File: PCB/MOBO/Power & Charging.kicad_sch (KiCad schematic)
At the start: 53 parts, among them J201 MAIN-USBC-OTG/PWR, Q201 AO3401A, Q202 FS8205A, Q203 IRLML6344, Q204 Si4435DDY, SW201 PCM12SMTR, U201 DW01A, U202 LC709203FQH-01TWG, U203 MCP73871-1AA, U204 TPS61230DRC

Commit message: added parts links in BOM
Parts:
- F201: footprint Fuse:Fuse_0805_2012Metric -> Fuse:Fuse_1206_3216Metric
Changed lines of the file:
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@@
       (effects (font (size 1.27 1.27)) hide)
     )
-    (property "Datasheet" "~" (at 179.07 209.55 0)
+    (property "Datasheet" "https://octopart.com/ncu18xh103f6srb-murata-75166631?r=sp" (at 179.07 209.55 0)
       (effects (font (size 1.27 1.27)) hide)
     )
@@
       (effects (font (size 1.27 1.27)) hide)
     )
-    (property "Datasheet" "~" (at 260.35 92.71 0)
+    (property "Datasheet" "https://octopart.com/pcm12smtr-c%26k+components-2486974?r=sp" (at 260.35 92.71 0)
       (effects (font (size 1.27 1.27)) hide)
     )
@@
       (effects (font (size 1.27 1.27)) hide)
     )
-    (property "Datasheet" "~" (at 196.85 69.85 0)
+    (property "Datasheet" "https://octopart.com/vaol-s8wr4-vcc-11855073?r=sp" (at 196.85 69.85 0)
       (effects (font (size 1.27 1.27)) hide)
     )
@@
       (effects (font (size 1.27 1.27)))
     )
-    (property "Footprint" "Fuse:Fuse_0805_2012Metric" (at 58.42 38.608 90)
-      (effects (font (size 1.27 1.27)) hide)
-    )
-    (property "Datasheet" "~" (at 58.42 36.83 0)
+    (property "Footprint" "Fuse:Fuse_1206_3216Metric" (at 58.42 38.608 90)
+      (effects (font (size 1.27 1.27)) hide)
+    )
+    (property "Datasheet" "https://octopart.com/0437002.wr-littelfuse-8600120?r=sp" (at 58.42 36.83 0)
       (effects (font (size 1.27 1.27)) hide)
     )
@@
       (effects (font (size 1.27 1.27)) hide)
     )
-    (property "Datasheet" "~" (at 179.07 68.58 0)
+    (property "Datasheet" "https://octopart.com/598-8191-107f-dialight-868609?r=sp" (at 179.07 68.58 0)
       (effects (font (size 1.27 1.27)) hide)
     )
@@
       (effects (font (size 1.27 1.27)) hide)
     )
-    (property "Datasheet" "https://www.usb.org/sites/default/files/documents/usb_type-c.zip" (at 31.75 52.07 0)
+    (property "Datasheet" "https://octopart.com/usb4085-gf-a-global+connector+technology-94773699?r=sp" (at 31.75 52.07 0)
       (effects (font (size 1.27 1.27)) hide)
     )
@@
       (effects (font (size 1.27 1.27)) hide)
     )
-    (property "Datasheet" "~" (at 134.62 91.44 0)
+    (property "Datasheet" "https://octopart.com/ncu18xh103f6srb-murata-75166631?r=sp" (at 134.62 91.44 0)
       (effects (font (size 1.27 1.27)) hide)
     )
@@
       (effects (font (size 1.27 1.27)) hide)
     )
-    (property "Datasheet" "~" (at 186.69 69.85 0)
-      (effects (font (size 1.27 1.27)) hide)
-    )
+    (property "Datasheet" "https://octopart.com/598-8120-107f-dialight-868603?r=sp" (at 186.69 69.85 0)
+      (effects (font (size 1.27 1.27)) hide)
+    )

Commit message: fixed schematic net names
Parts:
- J201: footprint Connector_USB:USB_C_Receptacle_GCT_USB4085 -> Connector_USB:USB_C_Receptacle_G-Switch_GT-USB-7010ASV
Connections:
- net +3V8: no longer C205.1, C206.1, Q204.5 (D), Q204.6 (D), Q204.7 (D), Q204.8 (D), R218.1, U203.1 (OUT), U203.20 (OUT)
- net +5V: no longer C202.1, F201.1, J201.A4 (VBUS), J201.A9 (VBUS), J201.B4 (VBUS), J201.B9 (VBUS), Q201.2 (S), R205.1, R207.1, U203.17 (CE), U203.18 (IN), U203.19 (IN), U203.4 (PROG2)
- net VPCC: now reaches R207.2, R208.1, U203.2 (VPCC)
- net PG: now reaches D203.2 (A), U203.6 (~{PG})
- net STAT2: now reaches D201.2 (A), U203.7 (STAT2)
- net STAT1: now reaches D202.2 (A), U203.8 (STAT1/~{LBO})
- net Latch Hold: now reaches D204.2 (A), Q203.1 (G), R217.2, R219.1
- net +5VA: now reaches D206.5 (VP), F201.2, Q201.3 (D)
- net Latch Enable: now reaches C206.2, D205.2 (A), Q203.3 (D), Q204.4 (G), R218.2
- net D+_IN: now reaches D206.1 (L1), J201.A7 (D-), J201.B7 (D-)
- net D-_IN: now reaches D206.3 (L2), J201.A6 (D+), J201.B6 (D+)
- new net +5VD: C202.1, Q201.2 (S), R205.1, R207.1, U203.17 (CE), U203.18 (IN), U203.19 (IN), U203.4 (PROG2)
- new net Charger 3V8 out: C205.1, C206.1, Q204.5 (D), Q204.6 (D), Q204.7 (D), Q204.8 (D), R218.1, U203.1 (OUT), U203.20 (OUT)
- new net VBUS: F201.1, J201.A4 (VBUS), J201.A9 (VBUS), J201.B4 (VBUS), J201.B9 (VBUS)
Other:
- moved on the sheet: R205

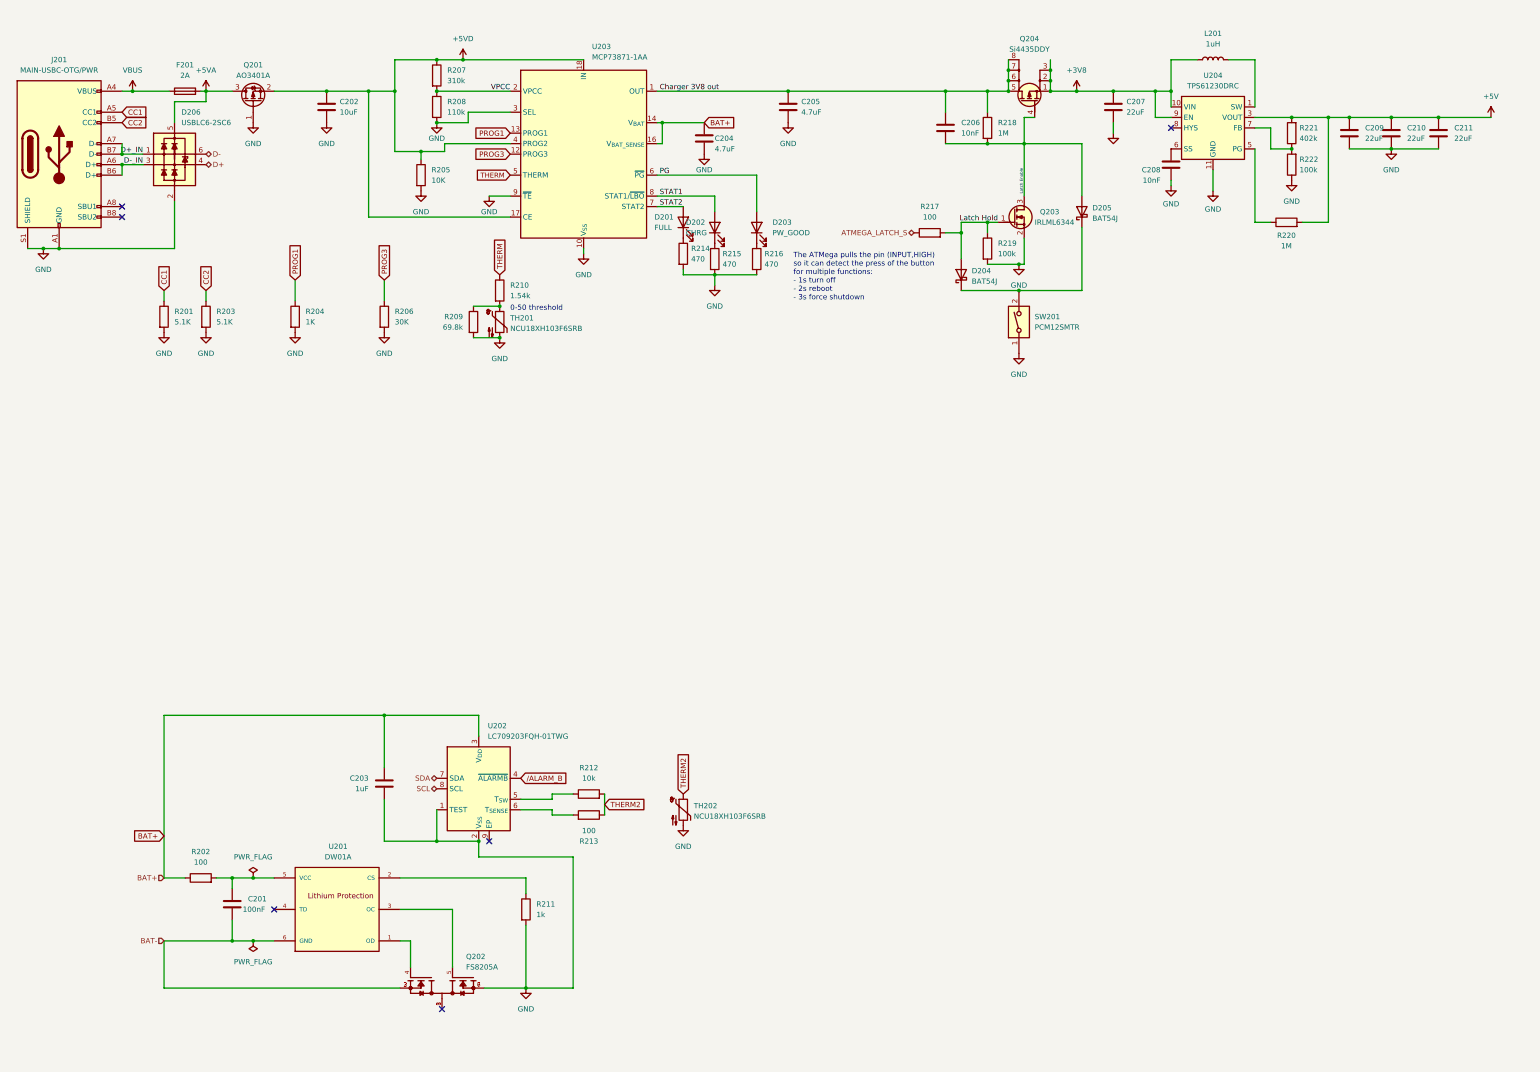
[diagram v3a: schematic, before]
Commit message: Started pcb traces
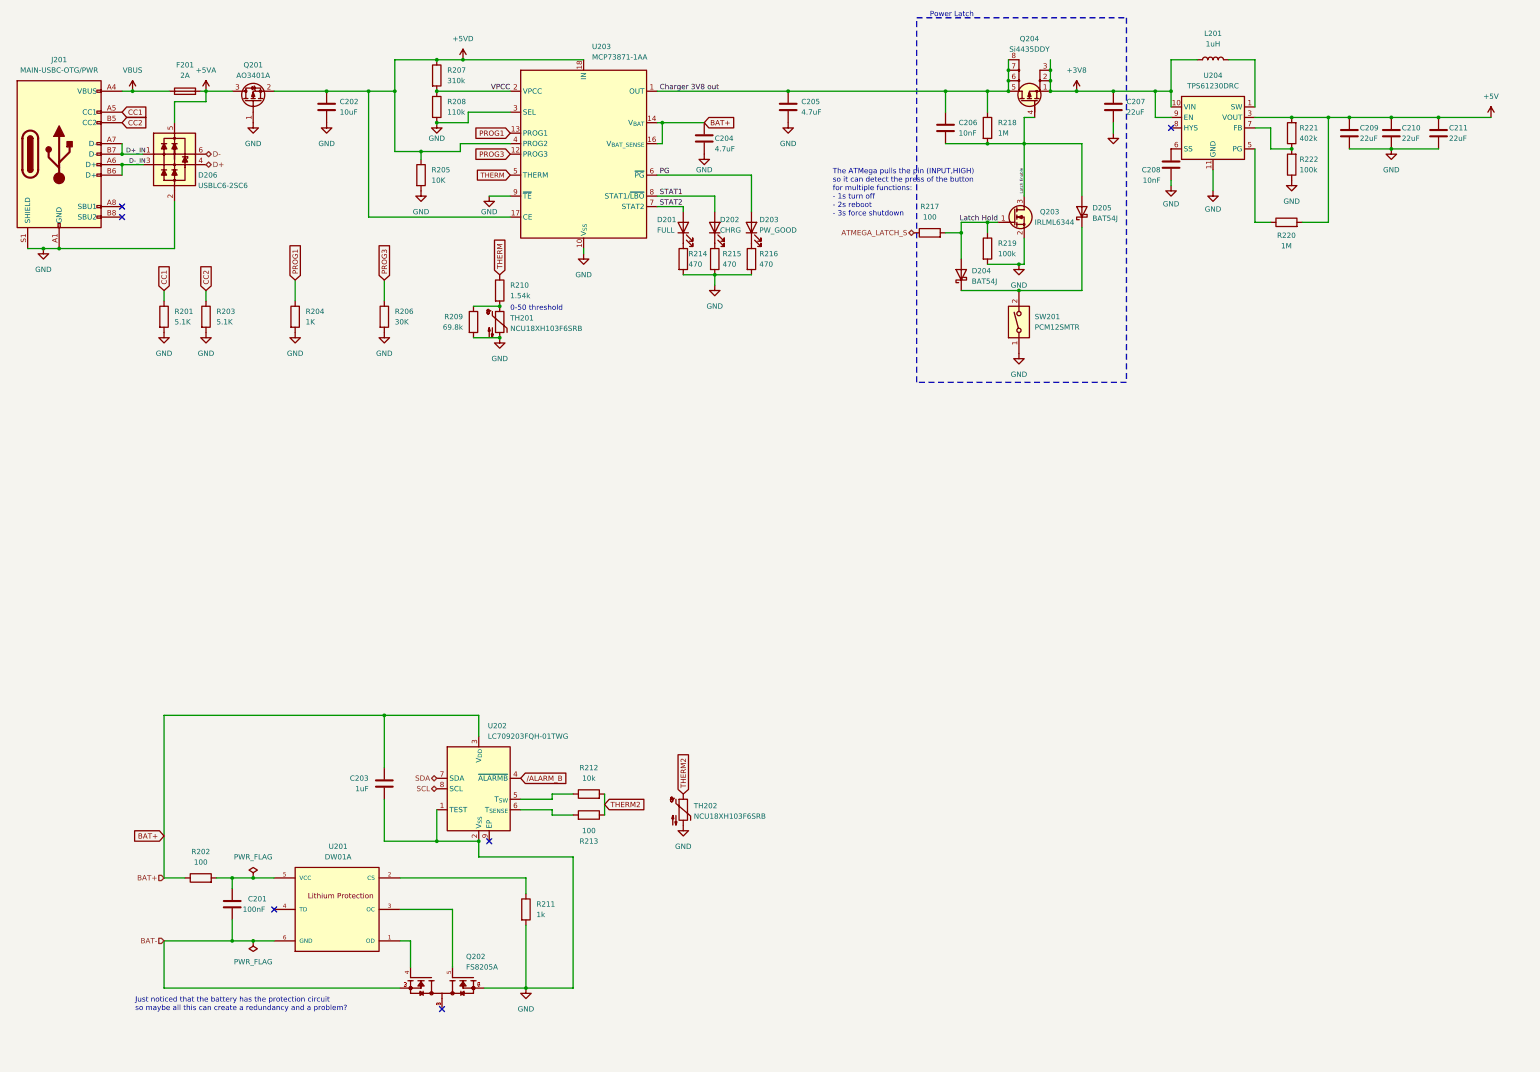
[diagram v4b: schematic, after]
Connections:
- net D+_IN: no longer D206.1 (L1), J201.A7 (D-), J201.B7 (D-)
- net D-_IN: no longer D206.3 (L2), J201.A6 (D+), J201.B6 (D+)
- new net: D206.1 (L1), J201.A7 (D-), J201.B7 (D-)
- new net: D206.3 (L2), J201.A6 (D+), J201.B6 (D+)
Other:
- note added: "Just noticed that the battery has the protection circuit so maybe all this can create a redundancy and a problem?"
- note added: "Power Latch"
- title: (none) -> Power & Charging
- moved on the sheet: D201, D203, R214, R216

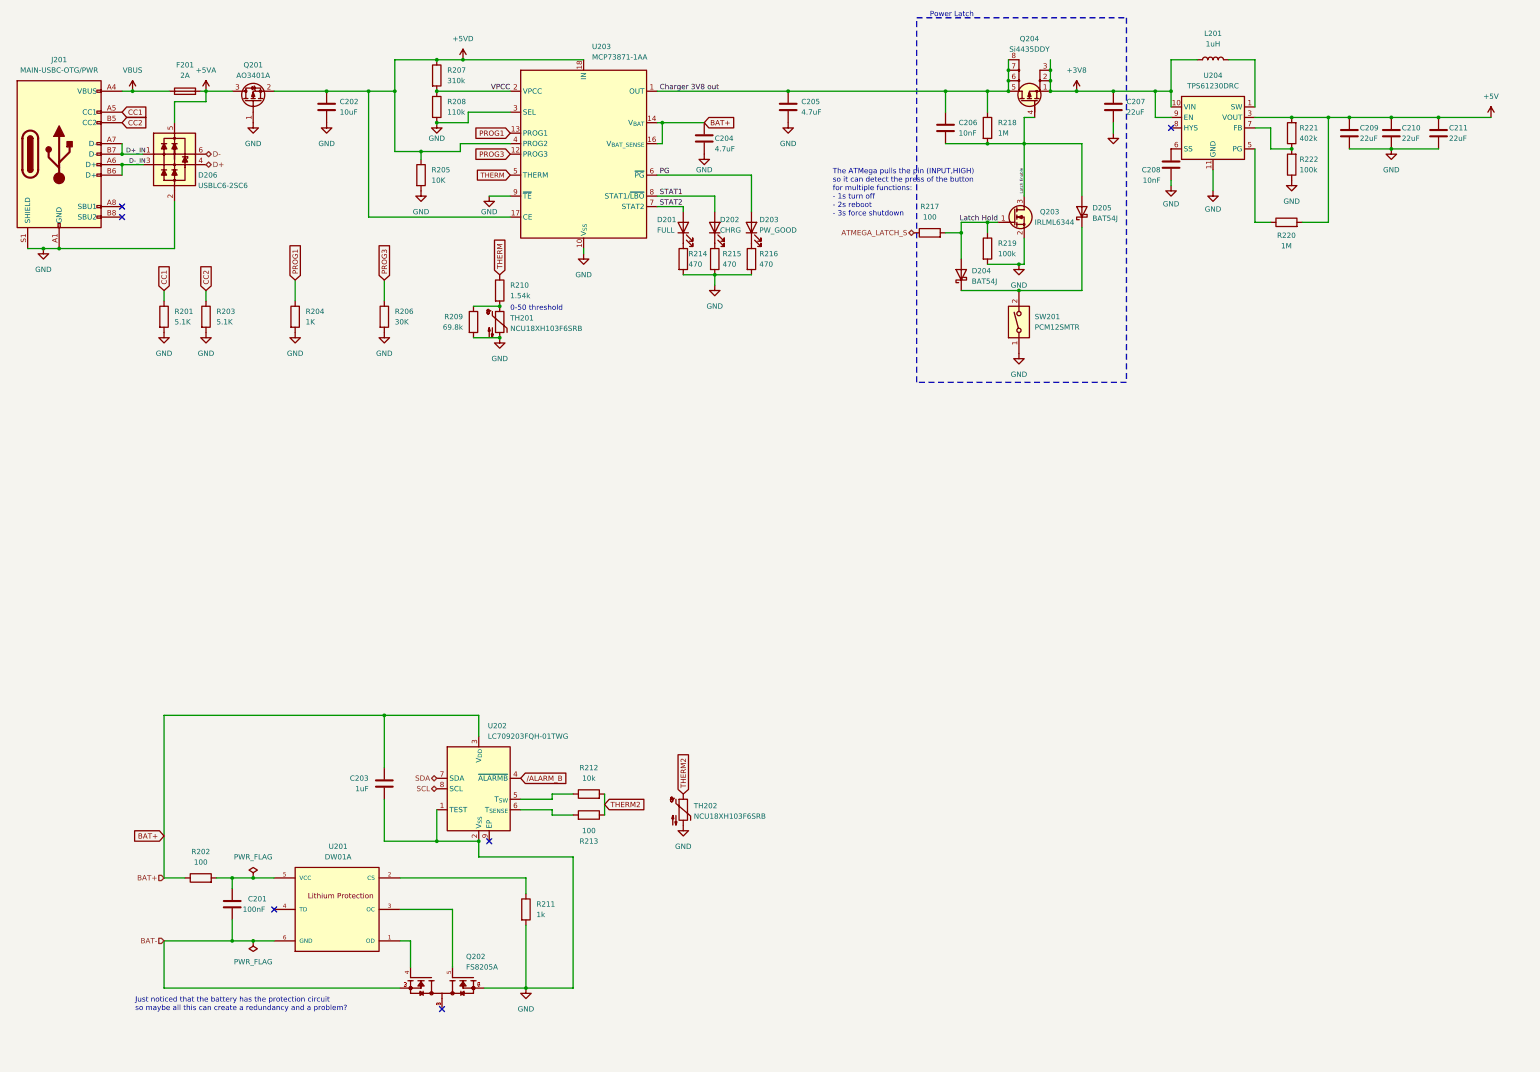
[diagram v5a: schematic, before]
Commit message: removed battery protection and gauge circuit
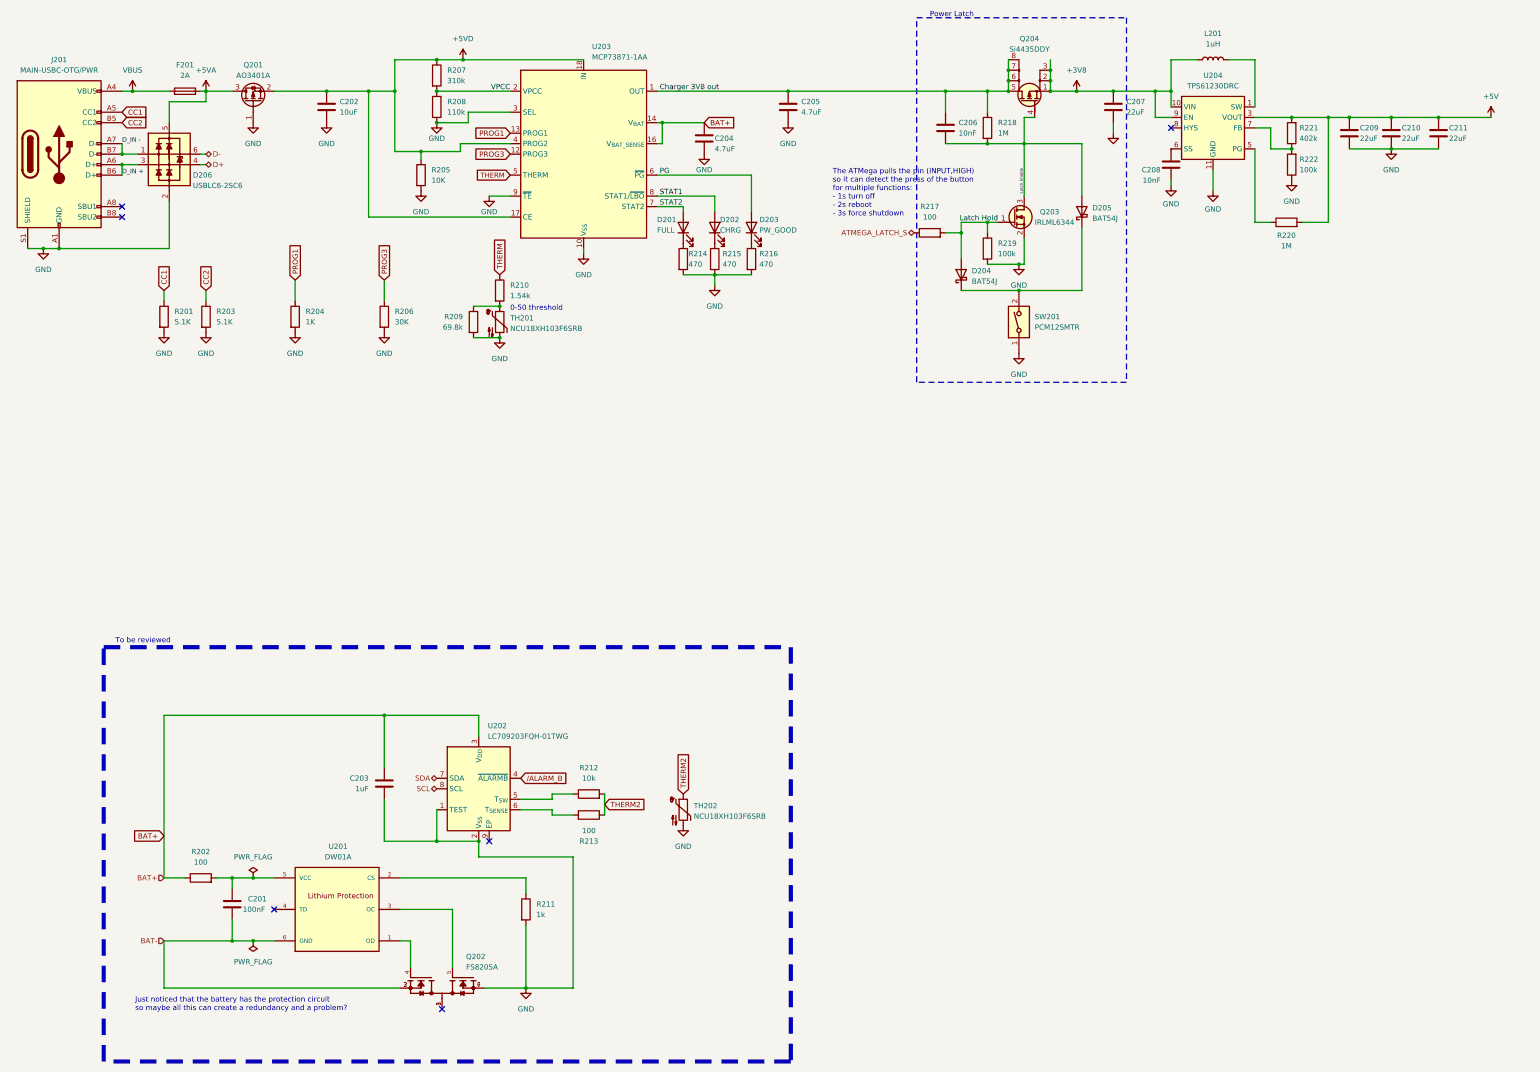
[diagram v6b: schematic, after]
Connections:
- net D_IN -: now reaches D206.1 (L1), J201.A7 (D-), J201.B7 (D-)
- net D_IN +: now reaches D206.3 (L2), J201.A6 (D+), J201.B6 (D+)
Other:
- note added: "To be reviewed"
- moved on the sheet: D206
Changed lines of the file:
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@@
 	)
 	(junction
+		(at 43.18 54.61)
+		(diameter 0)
+		(color 0 0 0 0)
+	)
+	(junction
 		(at 109.22 36.83)
 		(diameter 0)
@@
 	)
 	(junction
-		(at 43.18 54.61)
-		(diameter 0)
-		(color 0 0 0 0)
-	)
-	(junction
 		(at 350.52 43.18)
 		(diameter 0)
@@
 	(wire
 		(pts
+			(xy 62.23 52.07) (xy 63.5 52.07)
+		)
+		(stroke
+			(width 0)
+			(type default)
+		)
+	)
+	(wire
+		(pts
 			(xy 58.42 227.33) (xy 53.34 227.33)
 		)
@@
 	(wire
 		(pts
-			(xy 43.18 54.61) (xy 48.26 54.61)
-		)
-		(stroke
-			(width 0)
-			(type default)
-		)
-	)
-	(wire
-		(pts
 			(xy 139.7 208.28) (xy 147.32 208.28)
 		)
@@
 	(wire
 		(pts
-			(xy 43.18 52.07) (xy 48.26 52.07)
-		)
-		(stroke
-			(width 0)
-			(type default)
-		)
-	)
-	(wire
-		(pts
 			(xy 140.97 254) (xy 130.81 254)
 		)
@@
 	(wire
 		(pts
+			(xy 43.18 54.61) (xy 46.99 54.61)
+		)
+		(stroke
+			(width 0)
+			(type default)
+		)
+	)
+	(wire
+		(pts
 			(xy 172.72 62.23) (xy 186.69 62.23)
 		)
@@
 	(wire
 		(pts
-			(xy 55.88 74.93) (xy 55.88 63.5)
+			(xy 54.61 74.93) (xy 54.61 63.5)
 		)
 		(stroke
@@
 	(wire
 		(pts
+			(xy 43.18 52.07) (xy 46.99 52.07)
+		)
+		(stroke
+			(width 0)
+			(type default)
+		)
+	)
+	(wire
+		(pts
 			(xy 43.18 36.83) (xy 45.72 36.83)
 		)
@@
 	(wire
 		(pts
-			(xy 55.88 39.37) (xy 63.5 39.37)
+			(xy 54.61 39.37) (xy 63.5 39.37)
 		)
 		(stroke
@@
 	(wire
 		(pts
+			(xy 62.23 54.61) (xy 63.5 54.61)
+		)
+		(stroke
+			(width 0)
+			(type default)
+		)
+	)
+	(wire
+		(pts
 			(xy 43.18 54.61) (xy 43.18 57.15)
 		)
@@
 	(wire
 		(pts
-			(xy 55.88 39.37) (xy 55.88 44.45)
+			(xy 54.61 39.37) (xy 54.61 44.45)
 		)
 		(stroke
@@
 	(wire
 		(pts
-			(xy 27.94 74.93) (xy 55.88 74.93)
+			(xy 27.94 74.93) (xy 54.61 74.93)
 		)
 		(stroke
@@
 		)
 	)
+	(rectangle
+		(start 38.735 171.45)
+		(end 205.105 271.78)
+		(stroke
+			(width 1)
+			(type dash_dot_dot)
+			(color 255 0 2 1)
+		)
+		(fill
+			(type none)
+		)
+	)
 	(text "Power Latch "
 		(exclude_from_sim no)
@@
 		)
 	)
+	(text "To be reviewed\n"
+		(exclude_from_sim no)
+		(at 48.26 169.926 0)
+		(effects
+			(font
+				(size 1.27 1.27)
+			)
+		)
+	)
 	(text "0-50 threshold"
 		(exclude_from_sim no)
@@
 		)
 	)
-	(label "D-_IN"
-		(at 48.895 54.61 180)
+	(label "D_IN +"
+		(at 43.18 57.15 0)
 		(fields_autoplaced yes)
 		(effects
@@
 				(size 1.1 1.1)
 			)
-			(justify right bottom)
+			(justify left bottom)
 		)
 	)
@@
 		)
 	)
-	(label "D+_IN"
-		(at 48.895 52.07 180)
+	(label "D_IN -"
+		(at 43.18 49.53 0)
 		(fields_autoplaced yes)
 		(effects
@@
 				(size 1.1 1.1)
 			)
-			(justify right bottom)
+			(justify left bottom)
 		)
 	)
@@
 	(symbol
 		(lib_id "PCM_Diode_TVS_AKL:USBLC6-2SC6")
-		(at 55.88 52.07 0)
+		(at 54.61 52.07 0)
 		(unit 1)
 		(exclude_from_sim no)
@@
 		(dnp no)
 		(property "Reference" "D206"
-			(at 61.595 57.15 0)
+			(at 60.325 57.15 0)
 			(effects
 				(font
@@
 		)
 		(property "Value" "USBLC6-2SC6"
-			(at 61.595 59.69 0)
+			(at 60.325 59.69 0)
 			(effects
 				(font
@@
 		)
 		(property "Footprint" "Package_TO_SOT_SMD:SOT-23-6"
-			(at 55.88 52.07 0)
+			(at 54.61 52.07 0)
 			(effects
 				(font
@@
 		)
 		(property "Datasheet" "https://www.tme.eu/Document/db59d28d28a96c34f26d05f234ff409c/USBLC6-2.pdf"
-			(at 55.88 52.07 0)
+			(at 54.61 52.07 0)
 			(effects
 				(font
@@
 		)
 		(property "Description" ""
-			(at 55.88 52.07 0)
+			(at 54.61 52.07 0)
 			(effects
 				(font
